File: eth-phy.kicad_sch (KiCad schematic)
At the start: 1 part, among them U2 RTL8211FS-CG

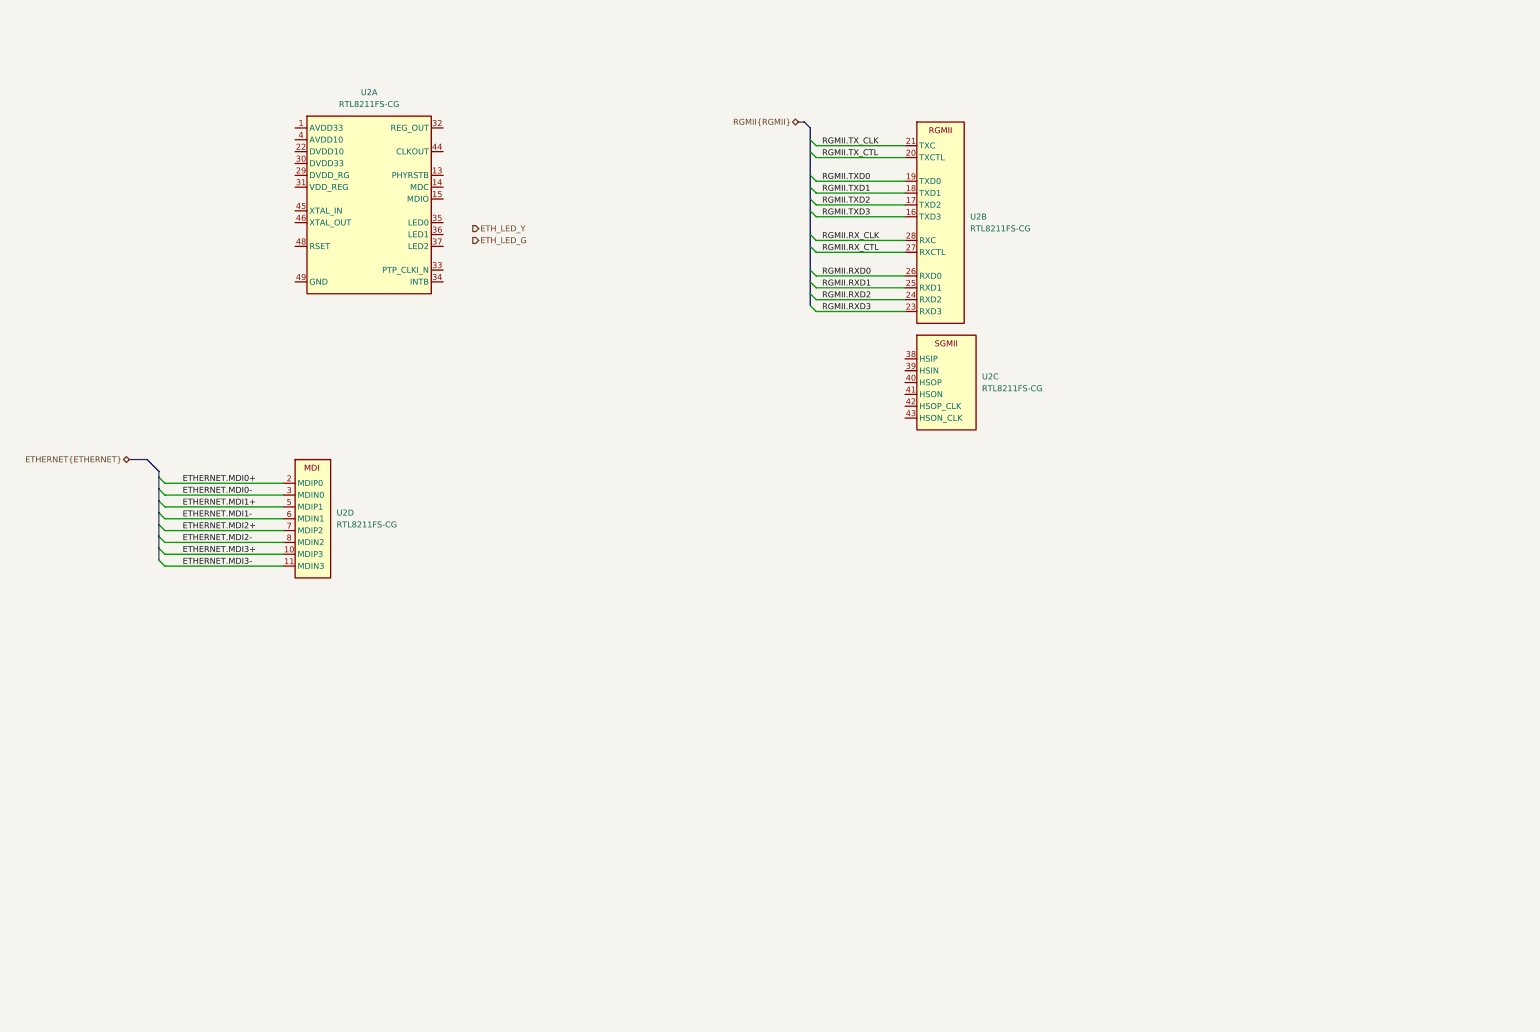
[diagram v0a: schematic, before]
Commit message: [#83329] Connect LEDs, crystal resontor, MDIO and MDC to the ETH PHY
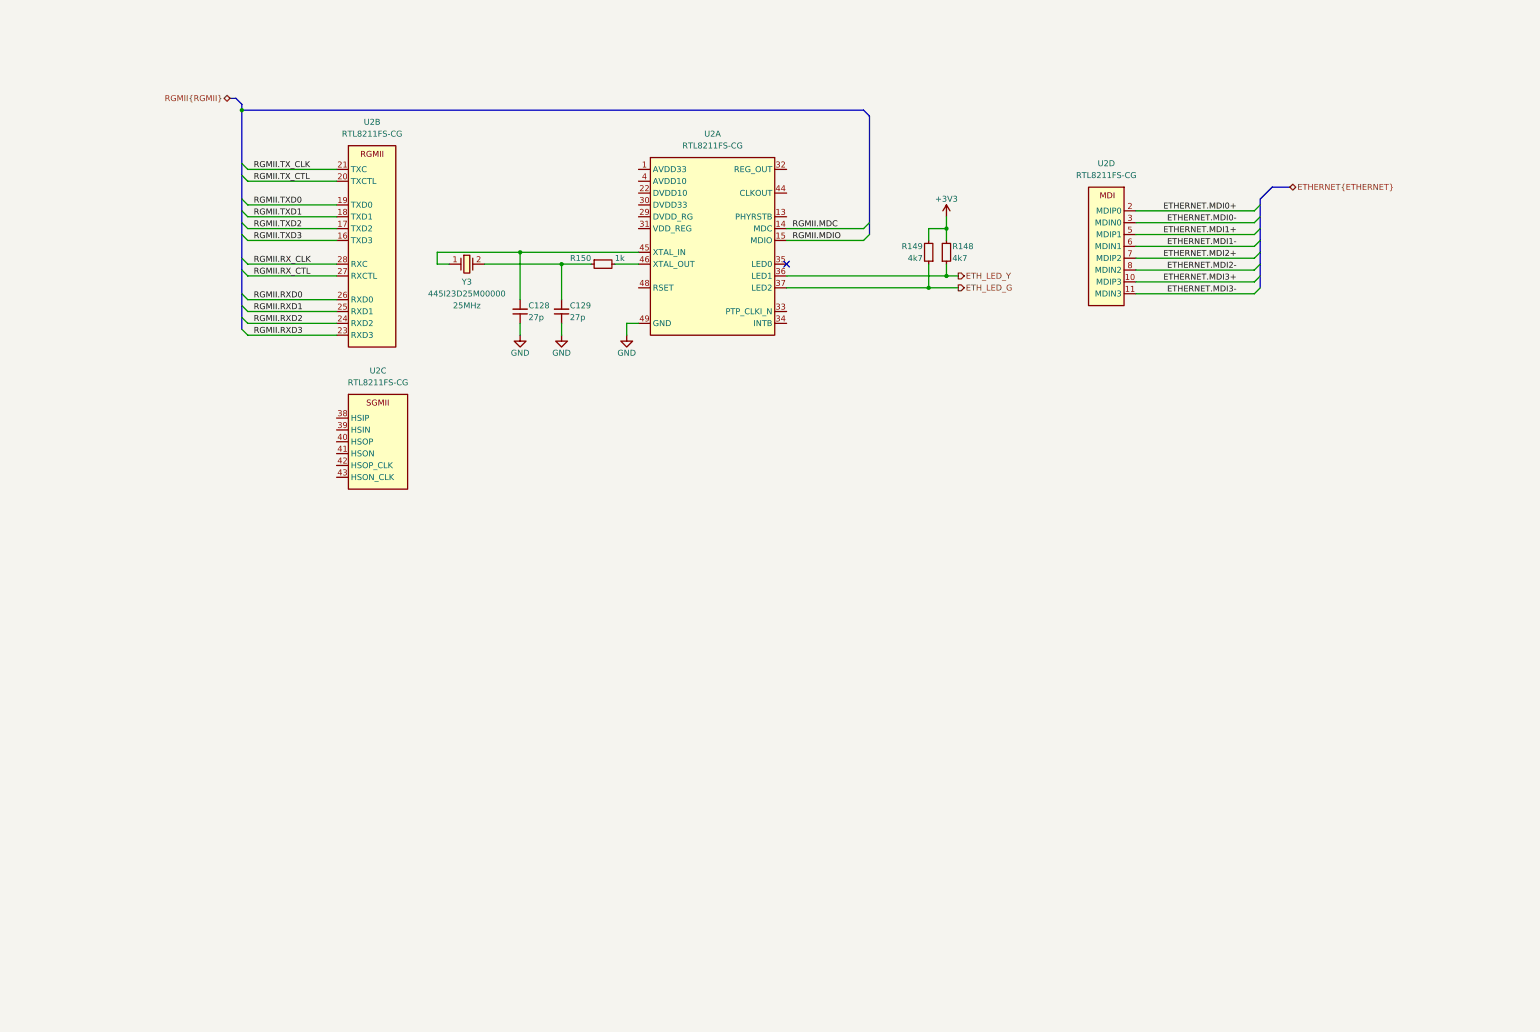
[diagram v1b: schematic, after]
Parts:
- added C128, C129: C_27p_0402, antmicro-footprints:C_0402_1005Metric, symbol antmicroCapacitors0402:C_27p_0402
- added R148, R149: R_4k7_0402, antmicro-footprints:R_0402_1005Metric, symbol antmicroResistors0402:R_4k7_0402
- added R150: R_1k_0402, antmicro-footprints:R_0402_1005Metric, symbol antmicroResistors0402:R_1k_0402
- added Y3: Resonator_25MHz_445, antmicro-footprints:Resonator_SMD_CTS_445_5x3.2mm, symbol antmicroResonators:Resonator_25MHz_445
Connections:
- net ETH_LED_G: now also U2.37 (LED2), R149.1
- net ETH_LED_Y: now also U2.36 (LED1), R148.1
- net RGMII.MDC: now reaches U2.14 (MDC)
- net RGMII.MDIO: now reaches U2.15 (MDIO)
- net at U2.45 (XTAL_IN): now also C128.2, Y3.1
- net at U2.46 (XTAL_OUT): now also R150.2
- net GND: now reaches U2.49 (GND)
- net GND: now also C128.1, C129.1
- new net: C129.2, R150.1, Y3.2
- new net +3V3: R148.2, R149.2
- no-connect marks 0 -> 1
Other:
- moved on the sheet: U2A, U2B, U2C, U2D

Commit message: [#83329] Connect power, and remaining signals
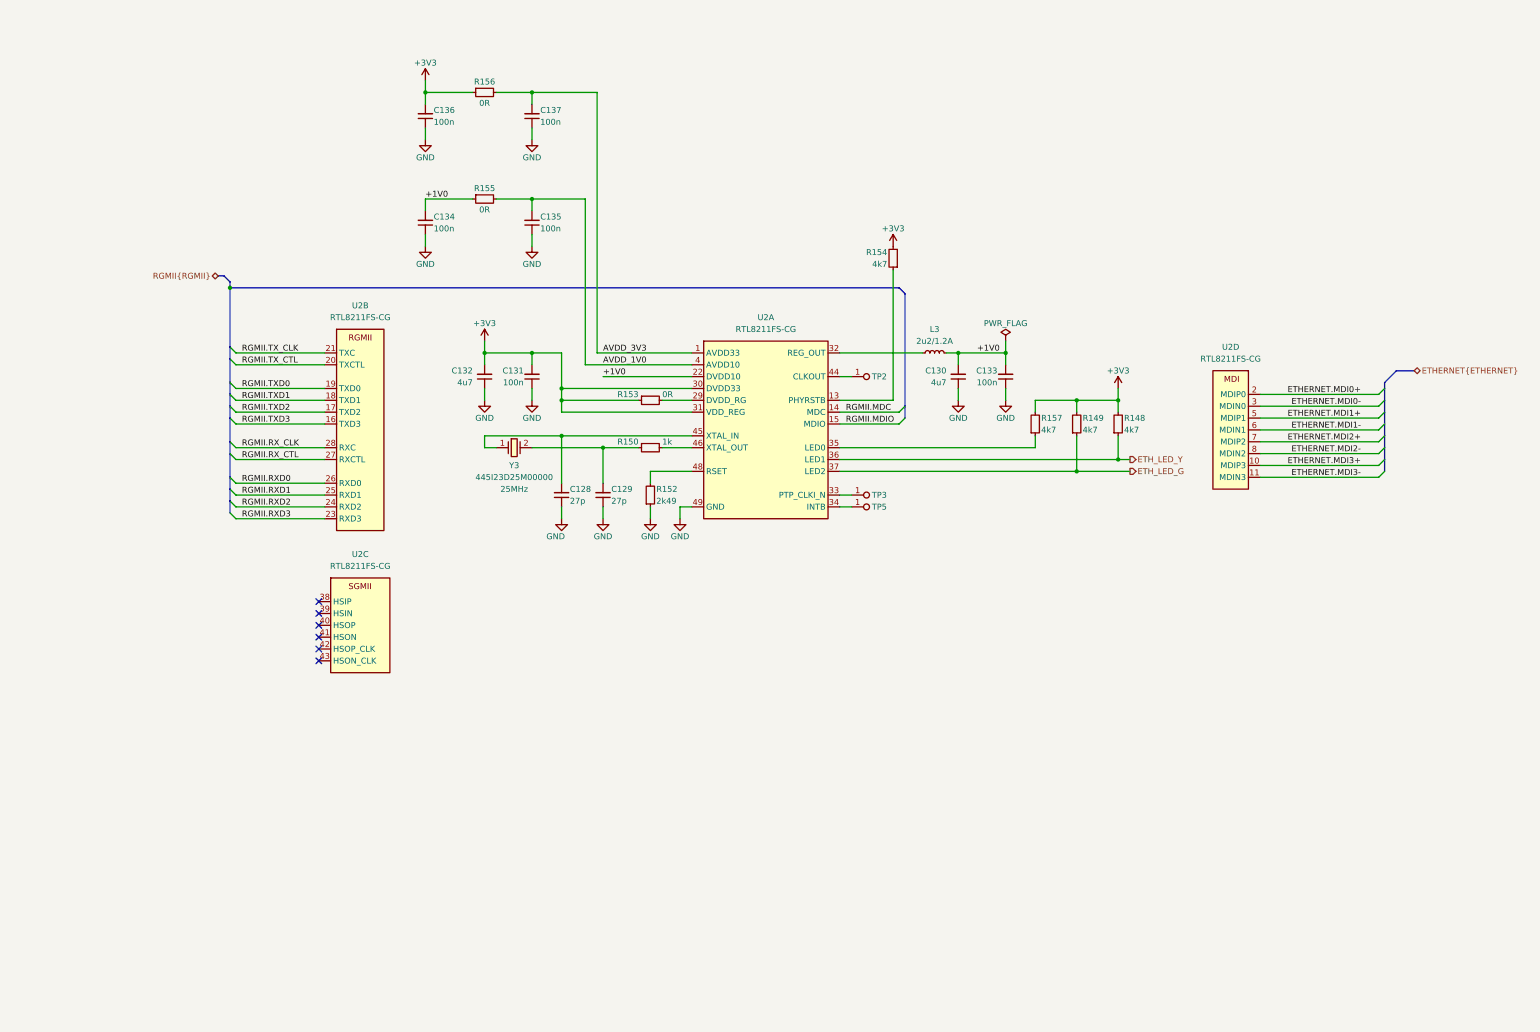
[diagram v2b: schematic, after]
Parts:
- added C130, C132: C_4u7_0402, antmicro-footprints:C_0402_1005Metric, symbol antmicroCapacitors0402:C_4u7_0402
- added C131, C133, C134, C135, C136, C137: C_100n_0402, antmicro-footprints:C_0402_1005Metric, symbol antmicroCapacitors0402:C_100n_0402
- added L3: L_2u2_1.2A_0603, antmicro-footprints:L_0603_1608Metric, symbol antmicroFixedInductors:L_2u2_1.2A_0603
- added R152: R_2k49_0402, antmicro-footprints:R_0402_1005Metric, symbol antmicroResistors0402:R_2k49_0402
- added R153, R155, R156: R_0R_0402, antmicro-footprints:R_0402_1005Metric, symbol antmicroResistors0402:R_0R_0402
- added R154, R157: R_4k7_0402, antmicro-footprints:R_0402_1005Metric, symbol antmicroResistors0402:R_4k7_0402
- added TP2, TP3, TP5: TP_0.75mm_SMD, antmicro-footprints:TP_SMD_0.75mm, symbol antmicroTestPoints:TP_0.75mm_SMD
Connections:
- net +3V3: now also U2.30 (DVDD33), U2.31 (VDD_REG), C131.2, C132.2, C136.2, R153.1, R154.2, R156.1, R157.2
- net GND: now also C130.1, C131.1, C132.1, C133.1, C134.1, C135.1, C136.1, C137.1, R152.1
- net AVDD_3V3: now reaches U2.1 (AVDD33), U2.12 (AVDD33), U2.30 (DVDD33)
- net AVDD_3V3: now also C137.2, R156.2
- net at U2.13 (PHYRSTB): now also R154.1
- net +1V0: now reaches U2.22 (DVDD10)
- net +1V0: now also C130.2, C133.2, C134.2, L3.2, R155.1
- net at U2.29 (DVDD_RG): now also R153.2
- net at U2.32 (REG_OUT): now also L3.1
- net at U2.33 (PTP_CLKI_N): now also TP3.1
- net at U2.34 (INTB): now also TP5.1
- net at U2.35 (LED0): now also R157.1
- net AVDD_1V0: now reaches U2.4 (AVDD10), U2.47 (AVDD10), U2.9 (AVDD10)
- net AVDD_1V0: now also C135.2, R155.2
- net at U2.44 (CLKOUT): now also TP2.1
- net at U2.48 (RSET): now also R152.2
- no-connect marks 1 -> 6
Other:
- moved on the sheet: C128, C129, R148, R149, R150, U2A, U2B, U2C, U2D, Y3

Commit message: [#83329] Change ETH PHY IC from RTL8211FS-CG to RTL8211FDI-CG
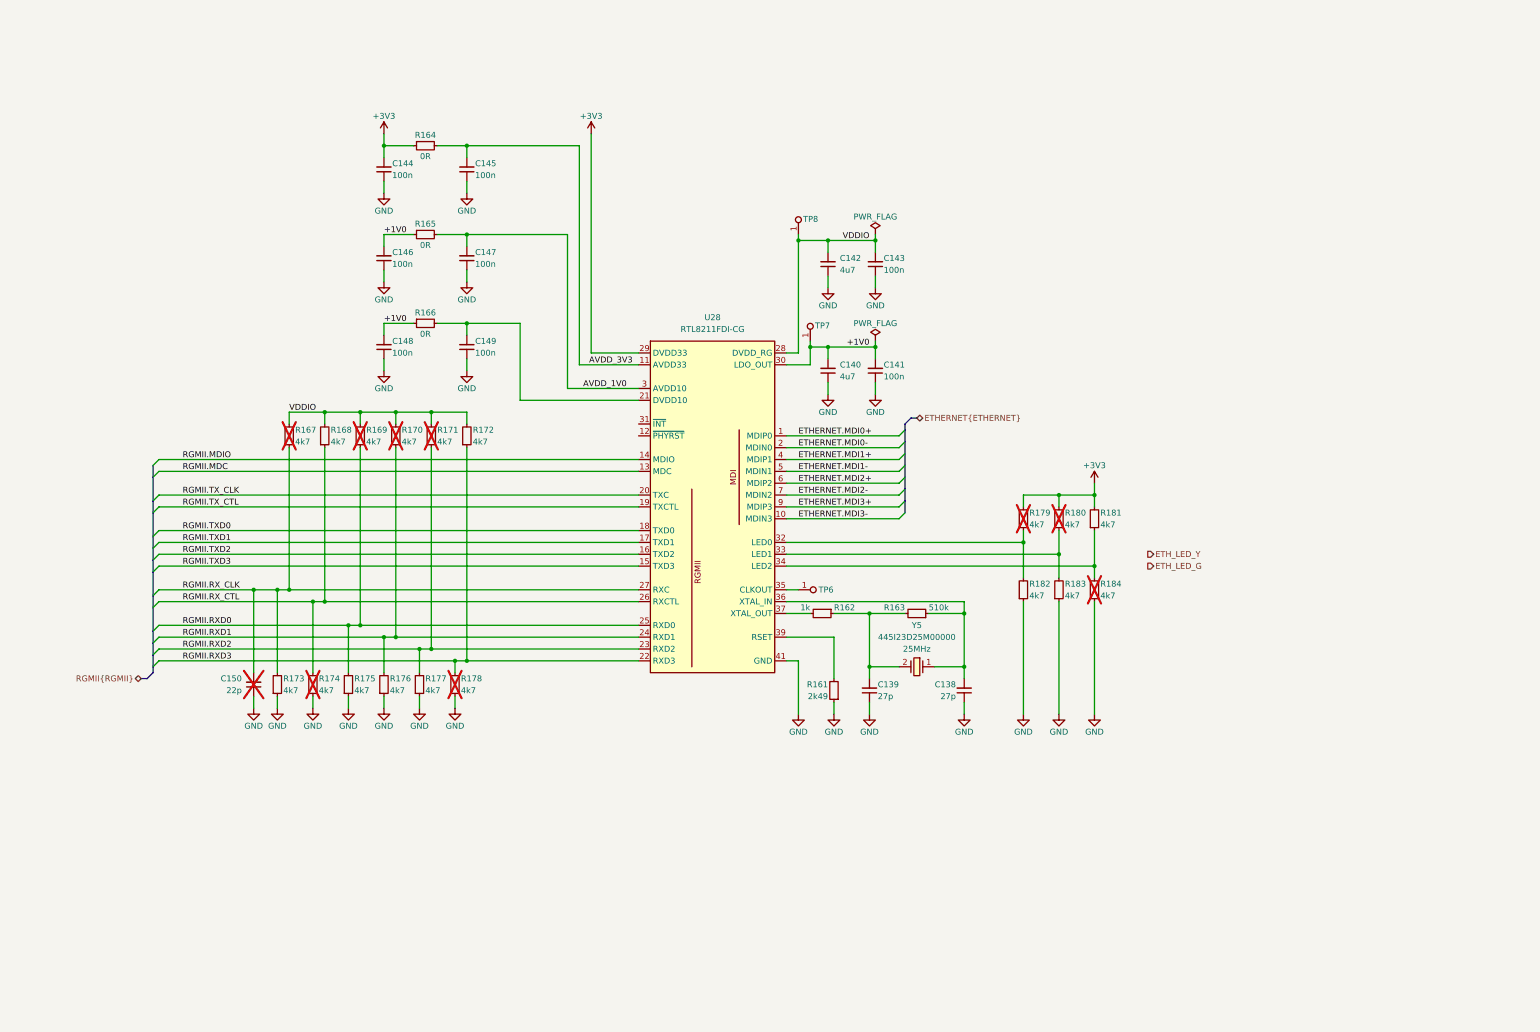
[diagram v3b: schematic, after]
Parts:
- removed C128, C129: C_27p_0402, antmicro-footprints:C_0402_1005Metric, symbol antmicroCapacitors0402:C_27p_0402
- removed C130, C132: C_4u7_0402, antmicro-footprints:C_0402_1005Metric, symbol antmicroCapacitors0402:C_4u7_0402
- removed C131, C133, C134, C135, C136, C137: C_100n_0402, antmicro-footprints:C_0402_1005Metric, symbol antmicroCapacitors0402:C_100n_0402
- removed L3: L_2u2_1.2A_0603, antmicro-footprints:L_0603_1608Metric, symbol antmicroFixedInductors:L_2u2_1.2A_0603
- removed R148, R149, R154, R157: R_4k7_0402, antmicro-footprints:R_0402_1005Metric, symbol antmicroResistors0402:R_4k7_0402
- removed R150: R_1k_0402, antmicro-footprints:R_0402_1005Metric, symbol antmicroResistors0402:R_1k_0402
- removed R152: R_2k49_0402, antmicro-footprints:R_0402_1005Metric, symbol antmicroResistors0402:R_2k49_0402
- removed R153, R155, R156: R_0R_0402, antmicro-footprints:R_0402_1005Metric, symbol antmicroResistors0402:R_0R_0402
- removed TP2, TP3, TP5: TP_0.75mm_SMD, antmicro-footprints:TP_SMD_0.75mm, symbol antmicroTestPoints:TP_0.75mm_SMD
- removed U2: RTL8211FS-CG, antmicro-footprints:QFN-48-1EP_6x6mm, symbol antmicroInterfaceControllers:RTL8211FS-CG
- removed Y3: Resonator_25MHz_445, antmicro-footprints:Resonator_SMD_CTS_445_5x3.2mm, symbol antmicroResonators:Resonator_25MHz_445
- added C138, C139: C_27p_0402, antmicro-footprints:C_0402_1005Metric, symbol antmicroCapacitors0402:C_27p_0402
- added C140, C142: C_4u7_0402, antmicro-footprints:C_0402_1005Metric, symbol antmicroCapacitors0402:C_4u7_0402
- added C141, C143, C144, C145, C146, C147, C148, C149: C_100n_0402, antmicro-footprints:C_0402_1005Metric, symbol antmicroCapacitors0402:C_100n_0402
- added C150: C_22p_0402, antmicro-footprints:C_0402_1005Metric, symbol antmicroCapacitors0402:C_22p_0402
- added R161: R_2k49_0402, antmicro-footprints:R_0402_1005Metric, symbol antmicroResistors0402:R_2k49_0402
- added R162: R_1k_0402, antmicro-footprints:R_0402_1005Metric, symbol antmicroResistors0402:R_1k_0402
- added R163: R_510k_0402, antmicro-footprints:R_0402_1005Metric, symbol antmicroResistors0402:R_510k_0402
- added R164, R165, R166: R_0R_0402, antmicro-footprints:R_0402_1005Metric, symbol antmicroResistors0402:R_0R_0402
- added R167, R168, R169, R170, R171, R172, R173, R174, R175, R176, R177, R178, R179, R180, R181, R182, R183, R184: R_4k7_0402, antmicro-footprints:R_0402_1005Metric, symbol antmicroResistors0402:R_4k7_0402
- added TP6, TP7, TP8: TP_0.75mm_SMD, antmicro-footprints:TP_SMD_0.75mm, symbol antmicroTestPoints:TP_0.75mm_SMD
- added U28: RTL8211FDI-CG, antmicro-footprints:UQFN-40-1EP_5x5mm_P0.4mm_EP3.8x3.8mm, symbol antmicroInterfaceControllers:RTL8211FDI-CG
- added Y5: Resonator_25MHz_445, antmicro-footprints:Resonator_SMD_CTS_445_5x3.2mm, symbol antmicroResonators:Resonator_25MHz_445
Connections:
- net +1V0: now also C140.2, C141.2, C146.2, C148.2, R165.1, R166.1, TP7.1, U28.30 (LDO_OUT)
- net +3V3: now also C144.2, R164.1, R179.2, R180.2, R181.2, U28.29 (DVDD33)
- net AVDD_1V0: now also C147.2, R165.2, U28.3 (AVDD10), U28.38 (AVDD10), U28.8 (AVDD10)
- net AVDD_3V3: now also C145.2, R164.2, U28.11 (AVDD33), U28.40 (AVDD33)
- net ETHERNET.MDI0+: now also U28.1 (MDIP0)
- net ETHERNET.MDI0-: now also U28.2 (MDIN0)
- net ETHERNET.MDI1+: now also U28.4 (MDIP1)
- net ETHERNET.MDI1-: now also U28.5 (MDIN1)
- net ETHERNET.MDI2+: now also U28.6 (MDIP2)
- net ETHERNET.MDI2-: now also U28.7 (MDIN2)
- net ETHERNET.MDI3+: now also U28.9 (MDIP3)
- net ETHERNET.MDI3-: now also U28.10 (MDIN3)
- net GND: now also C138.1, C139.1, C140.1, C141.1, C142.1, C143.1, C144.1, C145.1, C146.1, C147.1, C148.1, C149.1, C150.1, R161.1, R173.1, R174.1, R175.1, R176.1, R177.1, R178.1, R182.1, R183.1, R184.1, U28.41 (GND)
- net RGMII.MDC: now also U28.13 (MDC)
- net RGMII.MDIO: now also U28.14 (MDIO)
- net RGMII.RXD0: now also R169.1, R175.2, U28.25 (RXD0)
- net RGMII.RXD1: now also R170.1, R176.2, U28.24 (RXD1)
- net RGMII.RXD2: now also R171.1, R177.2, U28.23 (RXD2)
- net RGMII.RXD3: now also R172.1, R178.2, U28.22 (RXD3)
- net RGMII.RX_CLK: now also C150.2, R167.1, R173.2, U28.27 (RXC)
- net RGMII.RX_CTL: now also R168.1, R174.2, U28.26 (RXCTL)
- net RGMII.TXD0: now also U28.18 (TXD0)
- net RGMII.TXD1: now also U28.17 (TXD1)
- net RGMII.TXD2: now also U28.16 (TXD2)
- net RGMII.TXD3: now also U28.15 (TXD3)
- net RGMII.TX_CLK: now also U28.20 (TXC)
- net RGMII.TX_CTL: now also U28.19 (TXCTL)
- new net: C149.2, R166.2, U28.21 (DVDD10)
- new net: R179.1, R182.2, U28.32 (LED0)
- new net: R181.1, R184.2, U28.34 (LED2)
- new net: C138.2, R163.1, U28.36 (XTAL_IN), Y5.1
- new net: R180.1, R183.2, U28.33 (LED1)
- new net: TP6.1, U28.35 (CLKOUT)
- new net: R161.2, U28.39 (RSET)
- new net: C139.2, R162.1, R163.2, Y5.2
- new net: R162.2, U28.37 (XTAL_OUT)
- new net VDDIO: C142.2, C143.2, R167.2, R168.2, R169.2, R170.2, R171.2, R172.2, TP8.1, U28.28 (DVDD_RG)
- no-connect marks 6 -> 0
